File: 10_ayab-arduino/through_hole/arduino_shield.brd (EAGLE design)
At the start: 69.9 x 54.6 mm, 24 parts, among them IC3 MCP2300X/P, IC4 MCP2300X/P, X1 NEB1R

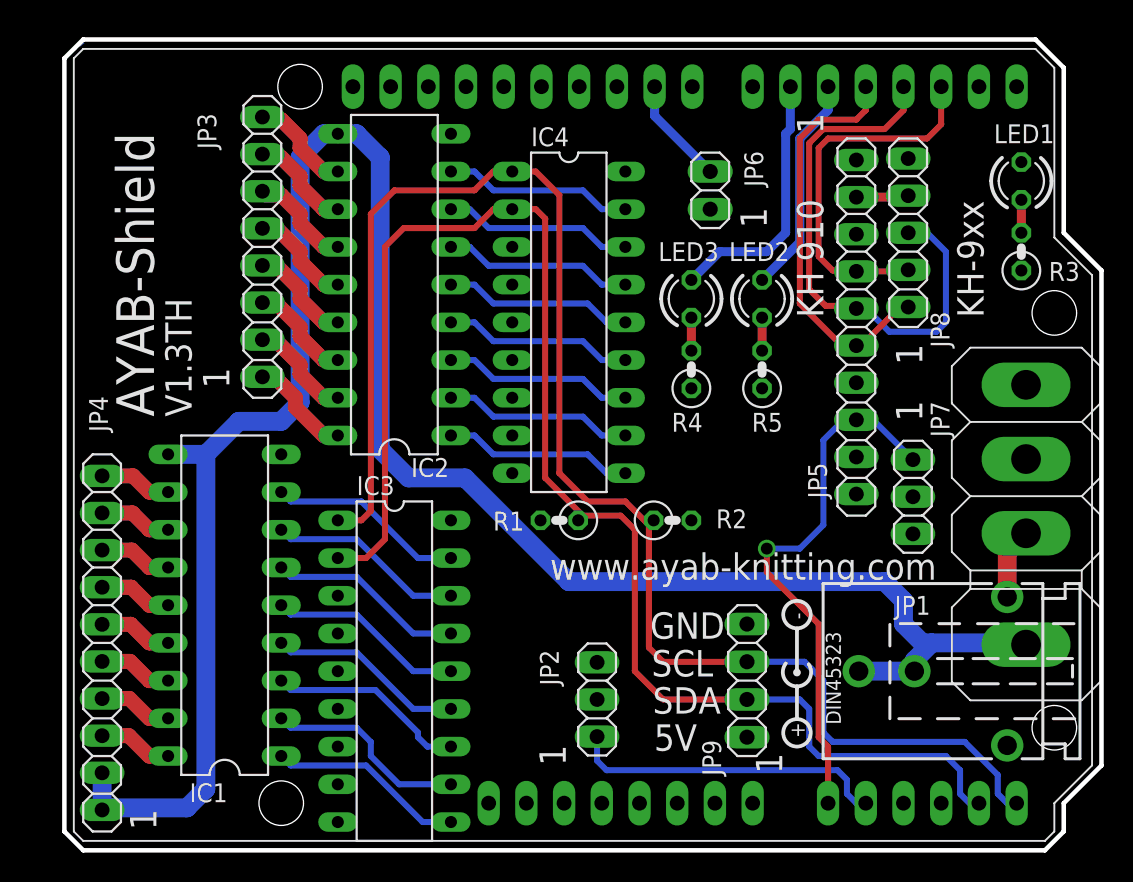
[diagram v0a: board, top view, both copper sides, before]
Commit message: /andz added 2mm holes for other machine types
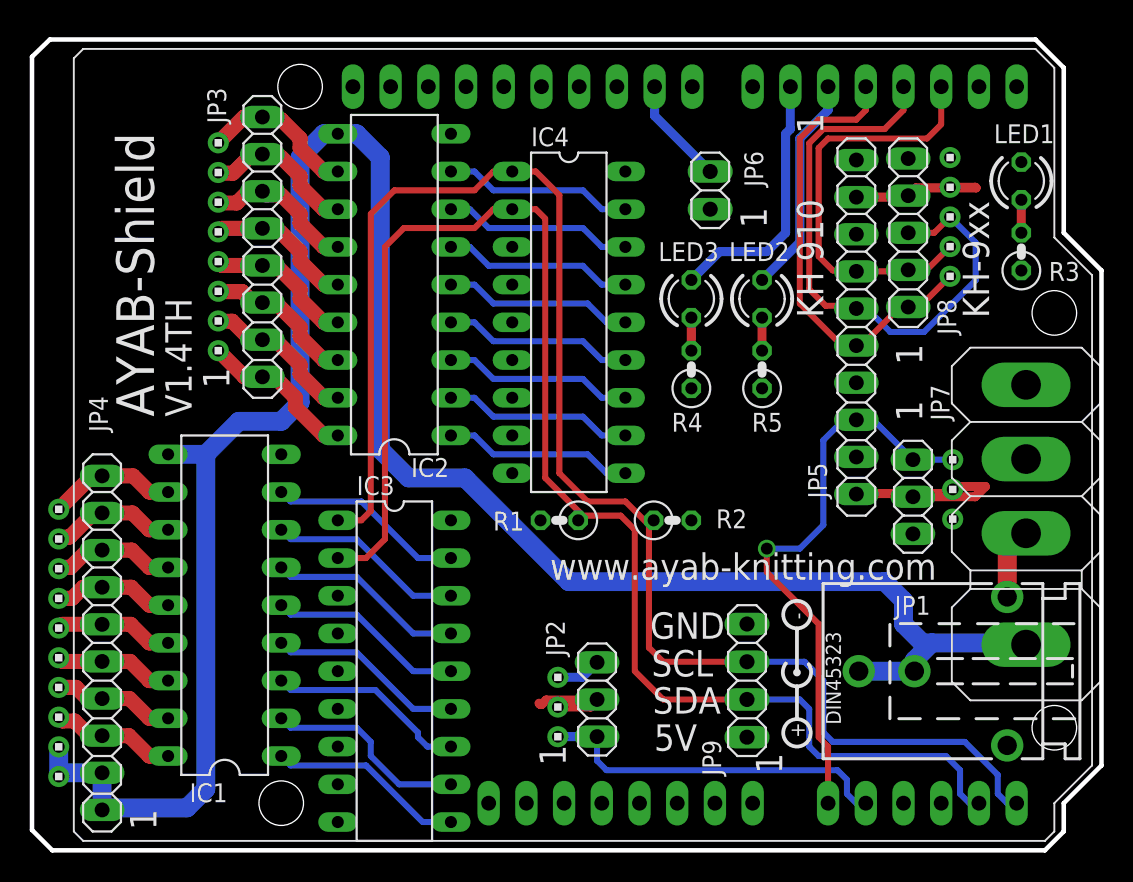
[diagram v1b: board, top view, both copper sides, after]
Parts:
- added JP2A, JP7A: 1X3, headers_2mm:1X3
- added JP3A: 1X8, headers_2mm:1X8
- added JP4A: 1X10, headers_2mm:1X10
- added JP8A: 1X5, headers_2mm:1X5
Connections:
- net +15V: now also JP4A.1, JP4A.2
- net +5V: now also JP2A.3, JP7A.3, JP8A.1
- net ENC0PINA: now also JP8A.4
- net ENC0PINB: now also JP8A.3
- net ENC0PINC: now also JP8A.5
- net EOL0L: now also JP2A.1
- net EOL0R: now also JP7A.1
- net GND: now also JP2A.2, JP7A.2, JP8A.2
- net N$17: now also JP3A.1
- net N$18: now also JP3A.2
- net N$19: now also JP3A.3
- net N$20: now also JP3A.4
- net N$21: now also JP3A.5
- net N$22: now also JP3A.6
- net N$23: now also JP3A.7
- net N$24: now also JP3A.8
- net N$25: now also JP4A.10
- net N$26: now also JP4A.9
- net N$27: now also JP4A.8
- net N$28: now also JP4A.7
- net N$29: now also JP4A.6
- net N$30: now also JP4A.5
- net N$31: now also JP4A.4
- net N$32: now also JP4A.3
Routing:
- net GND: track 8.35 -> 36.2 mm
- net +15V: track 142.0 -> 147.0 mm
- net N$25: track 4.90 -> 8.75 mm
- net N$17: track 7.09 -> 10.8 mm
- net N$24: track 6.97 -> 10.7 mm
- net ENC0PINC: track 27.5 -> 31.2 mm
- net N$26: track 4.91 -> 8.56 mm
- net ENC0PINB: track 37.2 -> 40.8 mm
- net N$23: track 6.99 -> 10.5 mm
- net N$18: track 7.07 -> 10.6 mm
- net +5V: track 0.00 -> 3.48 mm
- net ENC0PINA: track 25.2 -> 28.7 mm
- net N$27: track 4.93 -> 8.37 mm
- net N$32: track 5.01 -> 8.45 mm
- net N$22: track 7.01 -> 10.3 mm
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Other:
- board size 69.9 x 54.6 mm -> 72 x 54.6 mm
- board text added: "V1.4TH"
- board text removed: "V1.3TH"
